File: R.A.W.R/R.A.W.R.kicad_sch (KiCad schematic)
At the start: 97 parts, among them IC1 PSA4-5043+, IC2 ADE-1+, IC3 BQ24075QRGTRQ1, IC4 TPS61088RHLR, J1 BNC connector, J3 0.96 inch screen, SW3 RotaryEncoder_Switch, SW4 SW_SPST, U2 LM386, Y1 Si5351A-B-GT, Y2 25MHz

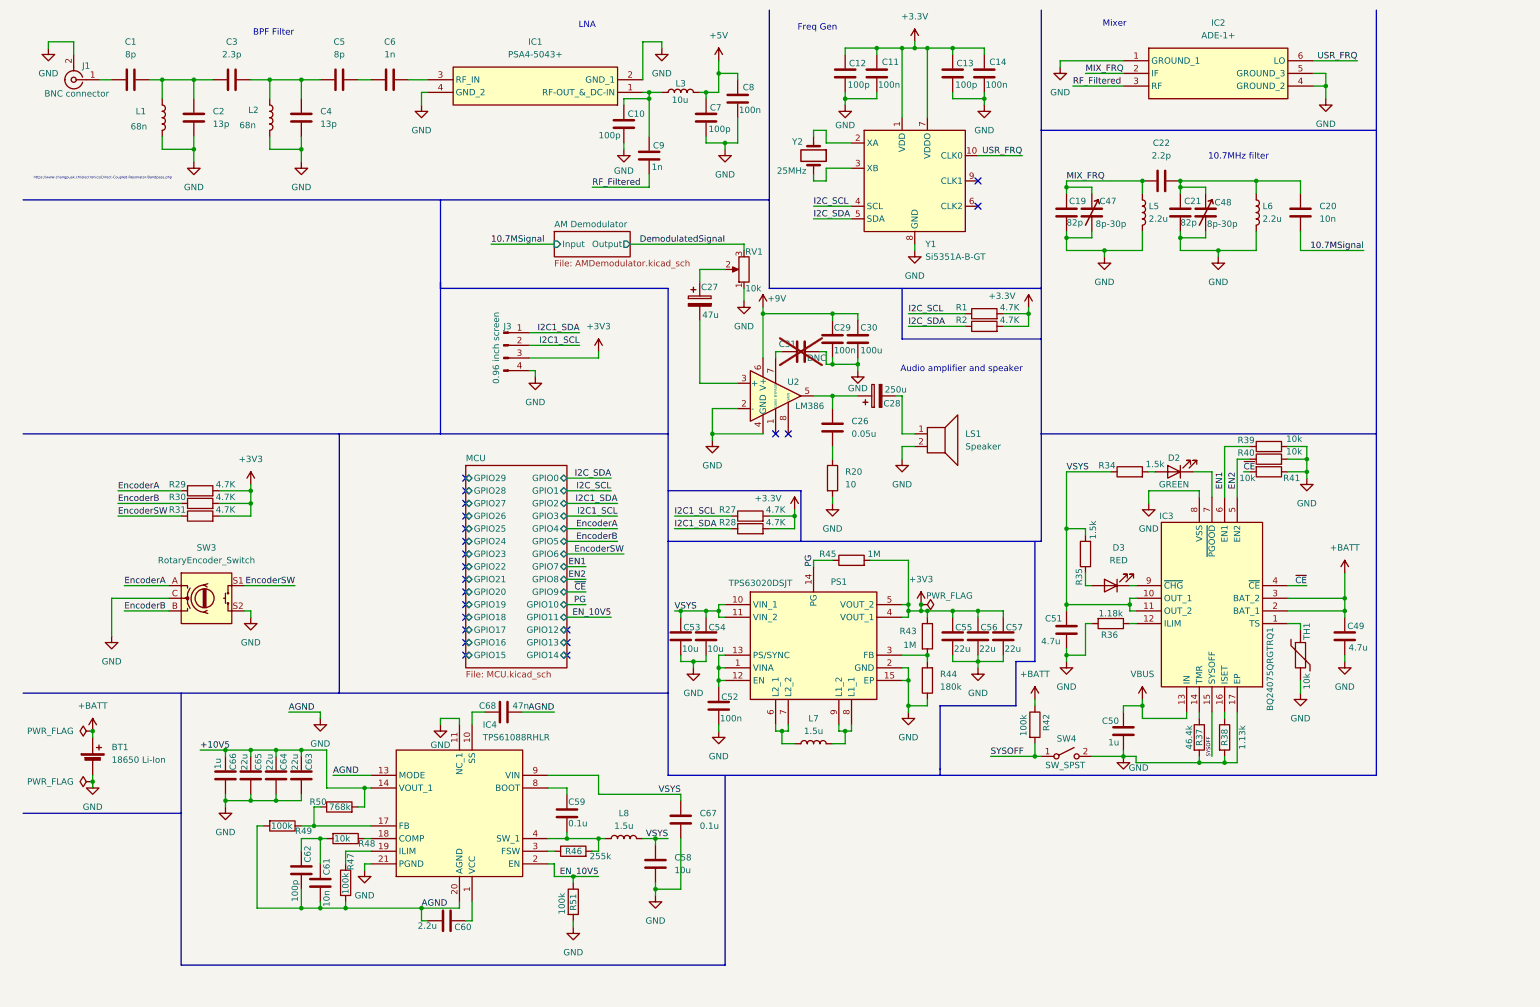
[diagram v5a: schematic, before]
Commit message: Finished adding footprints
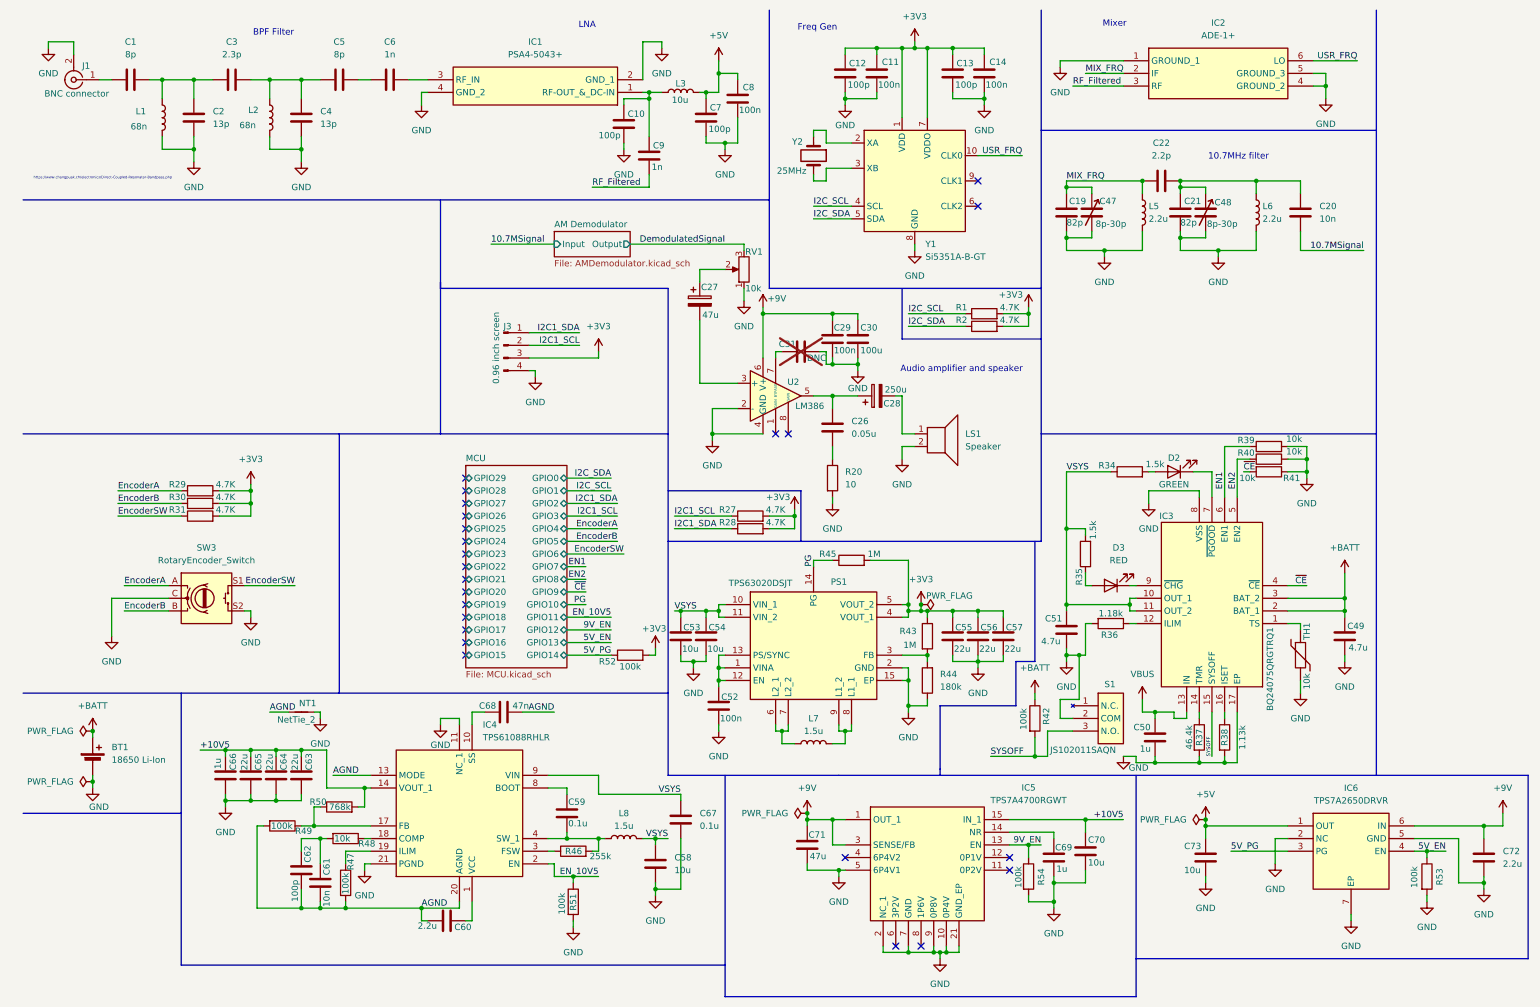
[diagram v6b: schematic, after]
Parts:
- removed SW4: SW_SPST, symbol Switch:SW_SPST
- added C69: 1u, Capacitor_SMD:C_0805_2012Metric_Pad1.18x1.45mm_HandSolder, symbol Device:C
- added C70, C73: 10u, Capacitor_SMD:C_0805_2012Metric_Pad1.18x1.45mm_HandSolder, symbol Device:C
- added C71: 47u, Capacitor_SMD:C_0805_2012Metric_Pad1.18x1.45mm_HandSolder, symbol Device:C
- added C72: 2.2u, Capacitor_SMD:C_0805_2012Metric_Pad1.18x1.45mm_HandSolder, symbol Device:C
- added IC5: TPS7A4700RGWT, RAWR:TPS7A4700RGWT, symbol RAWR:TPS7A4700RGWT
- added IC6: TPS7A2650DRVR, RAWR:TPS7A2650DRVR, symbol RAWR:TPS7A2650DRVR
- added NT1: NetTie_2, RF_Module:ST_SPBTLE, symbol Device:NetTie_2
- added R52, R53, R54: 100k, Resistor_SMD:R_0805_2012Metric_Pad1.20x1.40mm_HandSolder, symbol Device:R
- added S1: JS102011SAQN, RAWR:JS102011SAQN, symbol RAWR:JS102011SAQN
- C49, C50, C51, C52, C53, C54, C55, C56, C57, C58, C59, C60, C61, C62, C63, C64, C65, C66, C67, C68: footprint QFN50P300X300X100-17N-D -> Capacitor_SMD:C_0805_2012Metric_Pad1.18x1.45mm_HandSolder
- D2, D3: footprint (none) -> LED_SMD:LED_1206_3216Metric_Pad1.42x1.75mm_HandSolder
- IC1: footprint PSA45043 -> RAWR:PSA45043
- IC2: footprint ADE1 -> RAWR:ADE1
- IC3: footprint QFN50P300X300X100-17N-D -> RAWR:QFN50P300X300X100-17N-D
- IC4: footprint RHL(R-PVQFN-N20)_1 -> RAWR:TPS61088RHLR
- L7, L8: footprint SON50P300X400X100-15N-D -> Inductor_SMD:L_0805_2012Metric_Pad1.05x1.20mm_HandSolder
- PS1: footprint SON50P300X400X100-15N-D -> RAWR:TPS63020DSJT
- R34, R35, R36, R37, R38, R39, R40, R41, R42, R43, R44, R45, R46, R47, R48, R49, R50, R51: footprint (none) -> Resistor_SMD:R_0805_2012Metric_Pad1.20x1.40mm_HandSolder
- TH1: footprint (none) -> Connector_PinHeader_2.54mm:PinHeader_1x02_P2.54mm_Vertical
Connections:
- net +3.3V is gone; now on net +3V3: C11.2, C12.2, C13.2, C14.2, R1.2, R2.2, R27.2, R28.2, Y1.1 (VDD), Y1.7 (VDDO)
- net +10V5: now also IC4.16 (VOUT_3), C70.1, IC5.15 (IN_1), IC5.16 (IN_2)
- net +3V3: now also R52.2
- net +5V: now also C73.1, IC6.1 (OUT)
- net +9V: now also C71.1, C72.1, IC5.1 (OUT_1), IC5.20 (OUT_2), IC5.3 (SENSE/FB), IC6.6 (IN)
- net GND: now also C69.2, C70.2, C71.2, C72.2, C73.2, IC5.10 (0P4V), IC5.17 (NC_2), IC5.18 (NC_3), IC5.19 (NC_4), IC5.2 (NC_1), IC5.21 (GND_EP), IC5.5 (6P4V1), IC5.7 (GND), IC5.9 (0P8V), IC6.2 (NC), IC6.5 (GND), IC6.7 (EP), NT1.2, R53.2, R54.2, S1.2 (COM); no longer C60.2, C61.2, C62.2, C68.2, IC4.13 (MODE), IC4.20 (AGND), R47.2, R49.2
- net SYSOFF: now also S1.3 (N.O.)
- new net: C69.1, IC5.14 (NR)
- new net 5V_EN: IC6.4 (EN), R53.1
- new net 5V_PG: IC6.3 (PG), R52.1
- new net 9V_EN: IC5.13 (EN), R54.1
- new net AGND: C60.2, C61.2, C62.2, C68.2, IC4.13 (MODE), IC4.20 (AGND), NT1.1, R47.2, R49.2
- no-connect marks 22 -> 24
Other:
- moved on the sheet: C50, R42
